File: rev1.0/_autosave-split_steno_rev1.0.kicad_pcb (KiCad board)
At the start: 2 copper layers, 97.6 x 84.5 mm, 43 parts, among them J0 Audio-Jack-4, K0 KEYSW, K1 KEYSW, K10 KEYSW, K11 KEYSW, K12 KEYSW, K13 KEYSW, K14 KEYSW, K15 KEYSW, K16 KEYSW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

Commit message: reorganized schematic library and pro micro footprint
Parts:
- SW0: moved to B.Cu
- turned SW0 to 180 degrees
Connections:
- net Net-(U0-Pad1) renamed /tx
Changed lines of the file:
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@@
   (general
     (links 509)
-    (no_connects 68)
+    (no_connects 65)
     (area 101.128124 71.362499 198.909376 156.046876)
     (thickness 1.6)
@@
   (net 32 /c4)
   (net 33 "Net-(SW0-Pad1)")
-  (net 34 "Net-(U0-Pad1)")
+  (net 34 /tx)
   (net 35 "Net-(U0-Pad2)")
   (net 36 "Net-(U0-Pad7)")
@@
     (add_net /r2)
     (add_net /r3)
+    (add_net /tx)
     (add_net GND)
     (add_net "Net-(D0-Pad2)")
@@
     (add_net "Net-(K18-Pad2)")
     (add_net "Net-(SW0-Pad1)")
-    (add_net "Net-(U0-Pad1)")
     (add_net "Net-(U0-Pad13)")
     (add_net "Net-(U0-Pad14)")
@@
     (fp_line (start -12.7 -6.35) (end -12.7 -8.89) (layer B.SilkS) (width 0.381))
     (pad 1 thru_hole rect (at -13.97 -7.62 270) (size 1.7526 1.7526) (drill 1.0922) (layers *.Cu *.SilkS *.Mask)
-      (net 34 "Net-(U0-Pad1)"))
+      (net 34 /tx))
     (pad 2 thru_hole circle (at -11.43 -7.62 270) (size 1.7526 1.7526) (drill 1.0922) (layers *.Cu *.SilkS *.Mask)
       (net 35 "Net-(U0-Pad2)"))
@@
     )
   )
-  (module Keebio-Parts:SW_Tactile_SPST_Angled_MJTP1117 (layer F.Cu)
-    (at 149.424075 75.902668)
+  (module Keebio-Parts:SW_Tactile_SPST_Angled_MJTP1117 (layer B.Cu)
+    (at 149.424075 75.902668 180)
     (descr "tactile switch SPST right angle, PTS645VL39-2 LFS")
     (tags "tactile switch SPST angled PTS645VL39-2 LFS C&K Button")
-    (fp_text reference SW0 (at 2.5 1.68) (layer F.SilkS)
-      (effects (font (size 1 1) (thickness 0.15)))
-    )
-    (fp_text value SW_PUSH (at 2.5 5.38988) (layer F.Fab)
-      (effects (font (size 1 1) (thickness 0.15)))
-    )
-    (fp_line (start 1.05 -3.85) (end 1.05 -2.59) (layer F.Fab) (width 0.1))
-    (fp_line (start 3.95 -3.85) (end 3.95 -2.59) (layer F.Fab) (width 0.1))
-    (fp_line (start 1.05 -3.85) (end 3.95 -3.85) (layer F.Fab) (width 0.1))
-    (fp_line (start -0.84 0.97) (end -0.84 1.2) (layer F.SilkS) (width 0.12))
-    (fp_line (start 5.95 3.6) (end 5.95 0.86) (layer F.Fab) (width 0.1))
-    (fp_line (start -1.25 3.6) (end -0.95 3.6) (layer F.Fab) (width 0.1))
-    (fp_line (start -0.95 0.86) (end 5.95 0.86) (layer F.Fab) (width 0.1))
-    (fp_line (start 6.25 3.6) (end 6.25 -2.59) (layer F.Fab) (width 0.1))
-    (fp_line (start -2.25 -2.8) (end 7.3 -2.8) (layer F.CrtYd) (width 0.05))
-    (fp_line (start 7.3 -2.8) (end 7.3 4.45) (layer F.CrtYd) (width 0.05))
-    (fp_line (start 7.3 4.45) (end -2.25 4.45) (layer F.CrtYd) (width 0.05))
-    (fp_line (start -2.25 4.45) (end -2.25 -2.8) (layer F.CrtYd) (width 0.05))
-    (fp_line (start -1.36 -2.7) (end 6.36 -2.7) (layer F.SilkS) (width 0.12))
-    (fp_line (start 6.36 -2.7) (end 6.36 1.2) (layer F.SilkS) (width 0.12))
-    (fp_line (start -1.36 -2.7) (end -1.36 1.2) (layer F.SilkS) (width 0.12))
-    (fp_line (start -1.25 -2.59) (end 6.25 -2.59) (layer F.Fab) (width 0.1))
-    (fp_line (start -1.25 3.6) (end -1.25 -2.59) (layer F.Fab) (width 0.1))
-    (fp_line (start 5.95 3.6) (end 6.25 3.6) (layer F.Fab) (width 0.1))
-    (fp_line (start -0.95 3.6) (end -0.95 0.86) (layer F.Fab) (width 0.1))
-    (fp_line (start 5.84 0.97) (end 5.84 1.2) (layer F.SilkS) (width 0.12))
-    (fp_line (start 5.3 0.97) (end 5.84 0.97) (layer F.SilkS) (width 0.12))
-    (fp_line (start -0.84 0.97) (end -0.3 0.97) (layer F.SilkS) (width 0.12))
-    (fp_line (start 0.8 0.97) (end 4.2 0.97) (layer F.SilkS) (width 0.12))
-    (pad "" thru_hole circle (at 6.01 2.49) (size 2.1 2.1) (drill 1.3) (layers *.Cu *.Mask))
-    (pad 2 thru_hole circle (at 5 0) (size 1.75 1.75) (drill 0.99) (layers *.Cu *.Mask)
+    (fp_text reference SW0 (at 2.5 -1.68 180) (layer B.SilkS)
+      (effects (font (size 1 1) (thickness 0.15)) (justify mirror))
+    )
+    (fp_text value SW_PUSH (at 2.5 -5.38988 180) (layer B.Fab)
+      (effects (font (size 1 1) (thickness 0.15)) (justify mirror))
+    )
+    (fp_line (start 1.05 3.85) (end 1.05 2.59) (layer B.Fab) (width 0.1))
+    (fp_line (start 3.95 3.85) (end 3.95 2.59) (layer B.Fab) (width 0.1))
+    (fp_line (start 1.05 3.85) (end 3.95 3.85) (layer B.Fab) (width 0.1))
+    (fp_line (start -0.84 -0.97) (end -0.84 -1.2) (layer B.SilkS) (width 0.12))
+    (fp_line (start 5.95 -3.6) (end 5.95 -0.86) (layer B.Fab) (width 0.1))
+    (fp_line (start -1.25 -3.6) (end -0.95 -3.6) (layer B.Fab) (width 0.1))
+    (fp_line (start -0.95 -0.86) (end 5.95 -0.86) (layer B.Fab) (width 0.1))
+    (fp_line (start 6.25 -3.6) (end 6.25 2.59) (layer B.Fab) (width 0.1))
+    (fp_line (start -2.25 2.8) (end 7.3 2.8) (layer B.CrtYd) (width 0.05))
+    (fp_line (start 7.3 2.8) (end 7.3 -4.45) (layer B.CrtYd) (width 0.05))
+    (fp_line (start 7.3 -4.45) (end -2.25 -4.45) (layer B.CrtYd) (width 0.05))
+    (fp_line (start -2.25 -4.45) (end -2.25 2.8) (layer B.CrtYd) (width 0.05))
+    (fp_line (start -1.36 2.7) (end 6.36 2.7) (layer B.SilkS) (width 0.12))
+    (fp_line (start 6.36 2.7) (end 6.36 -1.2) (layer B.SilkS) (width 0.12))
+    (fp_line (start -1.36 2.7) (end -1.36 -1.2) (layer B.SilkS) (width 0.12))
+    (fp_line (start -1.25 2.59) (end 6.25 2.59) (layer B.Fab) (width 0.1))
+    (fp_line (start -1.25 -3.6) (end -1.25 2.59) (layer B.Fab) (width 0.1))
+    (fp_line (start 5.95 -3.6) (end 6.25 -3.6) (layer B.Fab) (width 0.1))
+    (fp_line (start -0.95 -3.6) (end -0.95 -0.86) (layer B.Fab) (width 0.1))
+    (fp_line (start 5.84 -0.97) (end 5.84 -1.2) (layer B.SilkS) (width 0.12))
+    (fp_line (start 5.3 -0.97) (end 5.84 -0.97) (layer B.SilkS) (width 0.12))
+    (fp_line (start -0.84 -0.97) (end -0.3 -0.97) (layer B.SilkS) (width 0.12))
+    (fp_line (start 0.8 -0.97) (end 4.2 -0.97) (layer B.SilkS) (width 0.12))
+    (pad "" thru_hole circle (at 6.01 -2.49 180) (size 2.1 2.1) (drill 1.3) (layers *.Cu *.Mask))
+    (pad 2 thru_hole circle (at 5 0 180) (size 1.75 1.75) (drill 0.99) (layers *.Cu *.Mask)
       (net 20 GND))
-    (pad 1 thru_hole circle (at 0 0) (size 1.75 1.75) (drill 0.99) (layers *.Cu *.Mask)
+    (pad 1 thru_hole circle (at 0 0 180) (size 1.75 1.75) (drill 0.99) (layers *.Cu *.Mask)
       (net 33 "Net-(SW0-Pad1)"))
-    (pad "" thru_hole circle (at -1 2.49) (size 2.1 2.1) (drill 1.3) (layers *.Cu *.Mask))
-    (pad "" np_thru_hole circle (at 2.5 -1.21) (size 1.2 1.2) (drill 1.2) (layers *.Cu *.Mask))
+    (pad "" thru_hole circle (at -1 -2.49 180) (size 2.1 2.1) (drill 1.3) (layers *.Cu *.Mask))
+    (pad "" np_thru_hole circle (at 2.5 1.21 180) (size 1.2 1.2) (drill 1.2) (layers *.Cu *.Mask))
     (model ${KISYS3DMOD}/Buttons_Switches_THT.3dshapes/SW_Tactile_SPST_Angled_PTS645Vx39-2LFS.wrl
       (at (xyz 0 0 0))

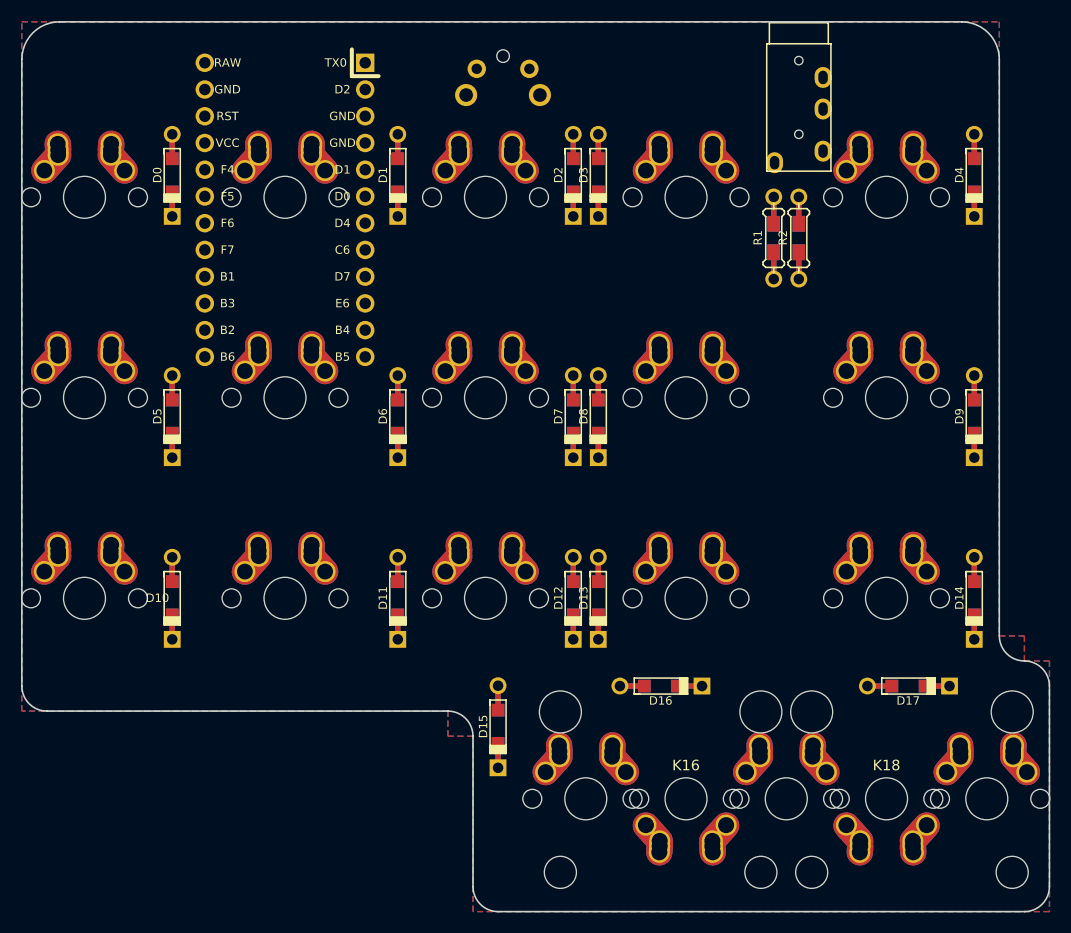
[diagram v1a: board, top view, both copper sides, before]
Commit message: removed global libraries and moved to local versions
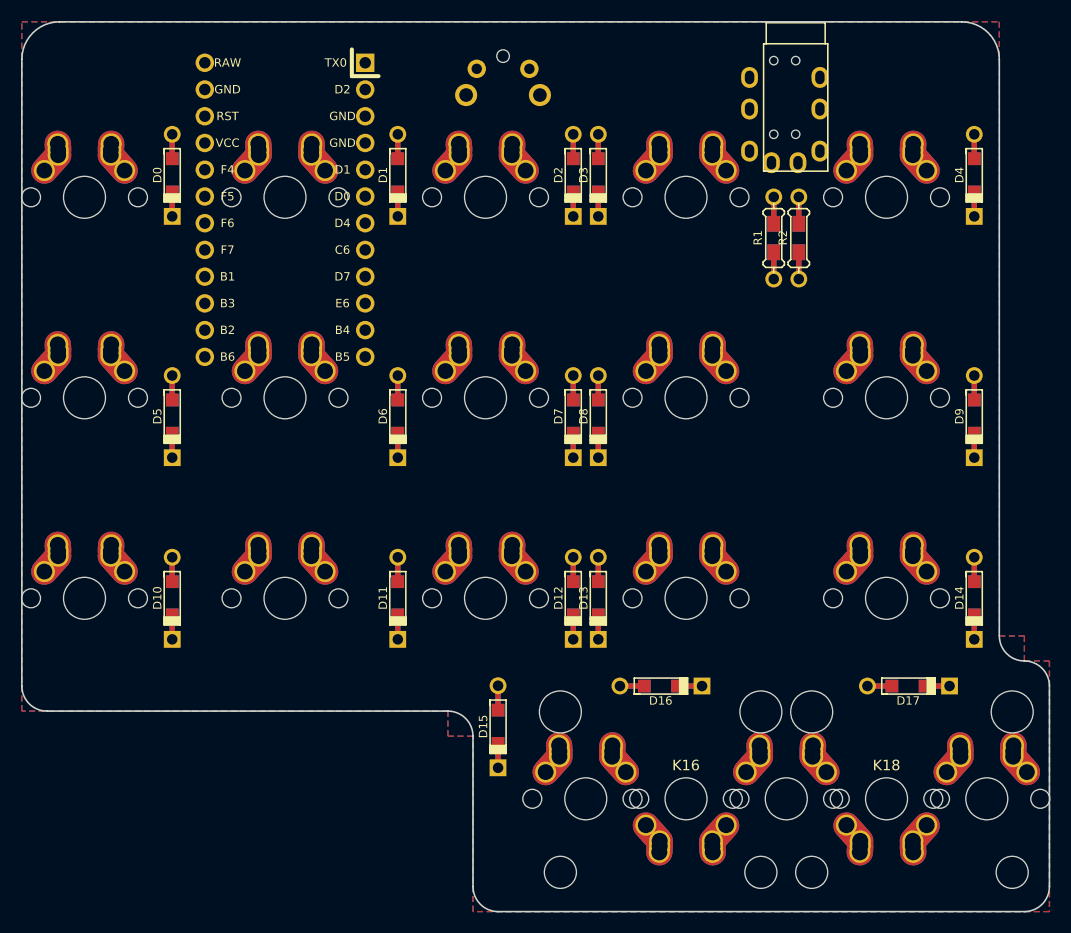
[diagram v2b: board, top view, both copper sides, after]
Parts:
- added REF**: TRRS-PJ-320A, Keebio-Parts:TRRS-PJ-320A, B.Cu at (172.6, 73.5)
- D0, D1, D10, D11, D12, D13, D14, D15, D16, D17, D2, D3, D4, D5, D6, D7, D8, D9: footprint Keebio-Parts:Diode-dual -> lib_fp:Diode-dual
- J0: value Audio-Jack-4 -> TRRS; footprint Keebio-Parts:TRRS-PJ-320A -> lib_fp:TRRS-PJ-320A
- K0, K1, K10, K11, K12, K13, K14, K15, K17, K19, K2, K3, K4, K5, K6, K7, K8, K9: footprint Keebio-Parts:Hybrid_PCB_100H_Dual_hole -> lib_fp:Hybrid_PCB_100H_Dual_hole
- K16, K18: footprint Keebio-Parts:Hybrid_PCB_200H-dual-nosilk -> lib_fp:Hybrid_PCB_200H-dual-nosilk
- R1, R2: footprint Keebio-Parts:Resistor-Hybrid -> lib_fp:Resistor-Hybrid
- SW0: footprint Keebio-Parts:SW_Tactile_SPST_Angled_MJTP1117 -> lib_fp:SW_Tactile_SPST_Angled_MJTP1117
- U0: footprint Keebio-Parts:ArduinoProMicro -> lib_fp:ArduinoProMicro
- moved J0 0.30 mm to (174.7, 73.5)
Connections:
- net /tx renamed Net-(U0-Pad1)
- J0 pad 3: VCC -> GND
- J0 pad 4: GND -> VCC
- K18 pad 2: Net-(K18-Pad2) -> Net-(D17-Pad2)
- R1 pad 1: VCC -> /d1
- R1 pad 2: /d1 -> VCC
- R2 pad 1: VCC -> /d0
- R2 pad 2: /d0 -> VCC
